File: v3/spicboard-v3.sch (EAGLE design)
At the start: 37 parts, among them IC1 74HC595N, Q1 BC557, Q2 BC557

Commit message: Zwischenstand LEDs
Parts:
- removed BUTTON0, BUTTON1: MOMENTARY-SWITCH-SPST-PTH-6.0MM, spicboard-v3:MOMENTARY-SWITCH-SPST-PTH-6.0MM
- added BTN0, BTN1: (no value), switch-omron:10-XX
- added R13, R14: 330, resistor:R-EU_0207/10
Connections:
- new net N$15: COM.1, R14.2
- new net N$21: COM.3, R13.2
- net BTN1: now also BTN1.S, BTN1.S1; no longer BUTTON1.2
- net GND: now also BTN0.P, BTN0.P1, BTN1.P, BTN1.P1; no longer BUTTON0.1, BUTTON1.1
- net N$19: now also BTN0.S, BTN0.S1; no longer BUTTON0.2
- net RX: now also R13.1; no longer COM.3
- net TX: now also R14.1; no longer COM.1
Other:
- moved on the sheet: COM, OLED2
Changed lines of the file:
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@@
 <part name="IC1" library="74xx-eu" deviceset="74*595" device="N" technology="HC"/>
 <part name="LDR" library="spicboard-v3" deviceset="LDR" device="LDR" value=""/>
-<part name="BUTTON0" library="spicboard-v3" deviceset="MOMENTARY-SWITCH-SPST" device="-PTH-6.0MM" value=""/>
-<part name="BUTTON1" library="spicboard-v3" deviceset="MOMENTARY-SWITCH-SPST" device="-PTH-6.0MM" value=""/>
 <part name="VR1" library="spicboard-v3" deviceset="POTENTIOMETER" device="-PTH-9MM-1/20W-20%" value="10k"/>
 <part name="RN1" library="resistor-sil" deviceset="E4R" device=""/>
@@
 <part name="OLED2" library="pinhead" deviceset="PINHD-1X4" device=""/>
 <part name="COM" library="pinhead" deviceset="PINHD-1X3" device=""/>
+<part name="R13" library="resistor" deviceset="R-EU_" device="0207/10" value="330"/>
+<part name="R14" library="resistor" deviceset="R-EU_" device="0207/10" value="330"/>
+<part name="BTN0" library="switch-omron" deviceset="10-XX" device=""/>
+<part name="BTN1" library="switch-omron" deviceset="10-XX" device=""/>
 </parts>
 <sheets>
@@
 <instance part="IC1" gate="A" x="109.22" y="40.64"/>
 <instance part="LDR" gate="G$1" x="83.82" y="101.6" rot="R90"/>
-<instance part="BUTTON0" gate="G$1" x="129.54" y="0" rot="R90"/>
-<instance part="BUTTON1" gate="G$1" x="172.72" y="0" rot="R90"/>
 <instance part="VR1" gate="G$1" x="63.5" y="96.52" rot="MR0"/>
 <instance part="RN1" gate="A" x="139.7" y="48.26"/>
@@
 <instance part="EXT" gate="A" x="48.26" y="-20.32"/>
 <instance part="OLED1" gate="A" x="48.26" y="-2.54"/>
-<instance part="OLED2" gate="A" x="68.58" y="-2.54"/>
-<instance part="COM" gate="A" x="68.58" y="-17.78"/>
+<instance part="OLED2" gate="A" x="81.28" y="-2.54"/>
+<instance part="COM" gate="A" x="81.28" y="-17.78"/>
+<instance part="R13" gate="G$1" x="68.58" y="-20.32"/>
+<instance part="R14" gate="G$1" x="68.58" y="-15.24"/>
+<instance part="BTN0" gate="1" x="129.54" y="0"/>
+<instance part="BTN1" gate="1" x="172.72" y="0"/>
 </instances>
 <busses>
@@
 <segment>
 <pinref part="OLED2" gate="A" pin="1"/>
-<wire x1="66.04" y1="2.54" x2="50.8" y2="2.54" width="0.1524" layer="91"/>
-<label x="50.8" y="2.54" size="1.778" layer="95"/>
+<wire x1="78.74" y1="2.54" x2="63.5" y2="2.54" width="0.1524" layer="91"/>
+<label x="63.5" y="2.54" size="1.778" layer="95"/>
 </segment>
 <segment>
@@
 </segment>
 <segment>
-<pinref part="BUTTON0" gate="G$1" pin="1"/>
 <wire x1="129.54" y1="-5.08" x2="129.54" y2="-7.62" width="0.1524" layer="91"/>
 <pinref part="GND7" gate="1" pin="GND"/>
-<wire x1="129.54" y1="-7.62" x2="137.16" y2="-7.62" width="0.1524" layer="91"/>
+<wire x1="129.54" y1="-7.62" x2="132.08" y2="-7.62" width="0.1524" layer="91"/>
+<wire x1="132.08" y1="-7.62" x2="137.16" y2="-7.62" width="0.1524" layer="91"/>
 <wire x1="137.16" y1="-7.62" x2="144.78" y2="-7.62" width="0.1524" layer="91"/>
 <junction x="137.16" y="-7.62"/>
@@
 <wire x1="144.78" y1="-7.62" x2="144.78" y2="-2.54" width="0.1524" layer="91"/>
 <wire x1="144.78" y1="-7.62" x2="172.72" y2="-7.62" width="0.1524" layer="91"/>
-<pinref part="BUTTON1" gate="G$1" pin="1"/>
 <wire x1="172.72" y1="-7.62" x2="172.72" y2="-5.08" width="0.1524" layer="91"/>
+<pinref part="BTN0" gate="1" pin="P"/>
+<pinref part="BTN1" gate="1" pin="P"/>
+<pinref part="BTN0" gate="1" pin="P1"/>
+<wire x1="132.08" y1="-5.08" x2="132.08" y2="-7.62" width="0.1524" layer="91"/>
+<junction x="132.08" y="-7.62"/>
+<pinref part="BTN1" gate="1" pin="P1"/>
+<wire x1="175.26" y1="-5.08" x2="175.26" y2="-7.62" width="0.1524" layer="91"/>
+<wire x1="175.26" y1="-7.62" x2="172.72" y2="-7.62" width="0.1524" layer="91"/>
+<junction x="172.72" y="-7.62"/>
 </segment>
 <segment>
@@
 <segment>
 <pinref part="OLED2" gate="A" pin="2"/>
-<wire x1="66.04" y1="0" x2="50.8" y2="0" width="0.1524" layer="91"/>
-<label x="50.8" y="0" size="1.778" layer="95"/>
+<wire x1="78.74" y1="0" x2="63.5" y2="0" width="0.1524" layer="91"/>
+<label x="63.5" y="0" size="1.778" layer="95"/>
 </segment>
 <segment>
 <pinref part="COM" gate="A" pin="2"/>
-<wire x1="66.04" y1="-17.78" x2="50.8" y2="-17.78" width="0.1524" layer="91"/>
-<label x="50.8" y="-17.78" size="1.778" layer="95"/>
+<wire x1="78.74" y1="-17.78" x2="55.88" y2="-17.78" width="0.1524" layer="91"/>
+<label x="55.88" y="-17.78" size="1.778" layer="95"/>
 </segment>
 <segment>
@@
 <net name="N$19" class="0">
 <segment>
-<pinref part="BUTTON0" gate="G$1" pin="2"/>
 <wire x1="129.54" y1="5.08" x2="129.54" y2="7.62" width="0.1524" layer="91"/>
 <pinref part="R12" gate="G$1" pin="1"/>
 <wire x1="129.54" y1="7.62" x2="132.08" y2="7.62" width="0.1524" layer="91"/>
+<pinref part="BTN0" gate="1" pin="S"/>
+<pinref part="BTN0" gate="1" pin="S1"/>
+<wire x1="132.08" y1="5.08" x2="132.08" y2="7.62" width="0.1524" layer="91"/>
+<junction x="132.08" y="7.62"/>
 </segment>
 </net>
@@
 <net name="BTN1" class="0">
 <segment>
-<pinref part="BUTTON1" gate="G$1" pin="2"/>
 <wire x1="172.72" y1="5.08" x2="172.72" y2="7.62" width="0.1524" layer="91"/>
-<wire x1="172.72" y1="7.62" x2="182.88" y2="7.62" width="0.1524" layer="91"/>
+<wire x1="172.72" y1="7.62" x2="175.26" y2="7.62" width="0.1524" layer="91"/>
 <label x="175.26" y="7.62" size="1.778" layer="95"/>
+<pinref part="BTN1" gate="1" pin="S"/>
+<pinref part="BTN1" gate="1" pin="S1"/>
+<wire x1="175.26" y1="7.62" x2="182.88" y2="7.62" width="0.1524" layer="91"/>
+<wire x1="175.26" y1="5.08" x2="175.26" y2="7.62" width="0.1524" layer="91"/>
+<junction x="175.26" y="7.62"/>
 </segment>
 <segment>
@@
 <net name="TX" class="0">
 <segment>
-<pinref part="COM" gate="A" pin="1"/>
-<wire x1="66.04" y1="-15.24" x2="50.8" y2="-15.24" width="0.1524" layer="91"/>
-<label x="50.8" y="-15.24" size="1.778" layer="95"/>
+<label x="55.88" y="-15.24" size="1.778" layer="95"/>
+<pinref part="R14" gate="G$1" pin="1"/>
+<wire x1="63.5" y1="-15.24" x2="55.88" y2="-15.24" width="0.1524" layer="91"/>
 </segment>
 <segment>
@@
 <net name="RX" class="0">
 <segment>
-<pinref part="COM" gate="A" pin="3"/>
-<wire x1="66.04" y1="-20.32" x2="50.8" y2="-20.32" width="0.1524" layer="91"/>
-<label x="50.8" y="-20.32" size="1.778" layer="95"/>
+<label x="55.88" y="-20.32" size="1.778" layer="95"/>
+<pinref part="R13" gate="G$1" pin="1"/>
+<wire x1="63.5" y1="-20.32" x2="55.88" y2="-20.32" width="0.1524" layer="91"/>
 </segment>
 <segment>
@@
 <segment>
 <pinref part="OLED2" gate="A" pin="4"/>
-<wire x1="66.04" y1="-5.08" x2="50.8" y2="-5.08" width="0.1524" layer="91"/>
-<label x="50.8" y="-5.08" size="1.778" layer="95"/>
+<wire x1="78.74" y1="-5.08" x2="63.5" y2="-5.08" width="0.1524" layer="91"/>
+<label x="63.5" y="-5.08" size="1.778" layer="95"/>
 </segment>
 </net>
@@
 <segment>
 <pinref part="OLED2" gate="A" pin="3"/>
-<wire x1="66.04" y1="-2.54" x2="50.8" y2="-2.54" width="0.1524" layer="91"/>
-<label x="50.8" y="-2.54" size="1.778" layer="95"/>
+<wire x1="78.74" y1="-2.54" x2="63.5" y2="-2.54" width="0.1524" layer="91"/>
+<label x="63.5" y="-2.54" size="1.778" layer="95"/>
 </segment>
 </net>
@@
 </segment>
 </net>
+<net name="N$15" class="0">
+<segment>
+<pinref part="COM" gate="A" pin="1"/>
+<wire x1="78.74" y1="-15.24" x2="73.66" y2="-15.24" width="0.1524" layer="91"/>
+<pinref part="R14" gate="G$1" pin="2"/>
+</segment>
+</net>
+<net name="N$21" class="0">
+<segment>
+<pinref part="COM" gate="A" pin="3"/>
+<wire x1="78.74" y1="-20.32" x2="73.66" y2="-20.32" width="0.1524" layer="91"/>
+<pinref part="R13" gate="G$1" pin="2"/>
+</segment>
+</net>

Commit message: Routing Zwischenstand
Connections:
- net IRQ renamed EXTIRQ
- removed net ADC: EXT.4
- new net EXTADC: B1.A3, EXT.4
- net L0: now also B1.*D6
- net L1: now also B1.*D5
- net L2: now also B1.D4
- net L3: now also B1.D7
- net L4: now also B1.D8
- net L5: now also B1.*D9
- net L6: now also B1.D12
- net L7: now also B1.A2
- net SS: now also IC1A.RCK
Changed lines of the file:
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@@
 <label x="22.86" y="78.74" size="1.778" layer="95"/>
+</segment>
+<segment>
+<pinref part="B1" gate="G$1" pin="*D6"/>
+<wire x1="76.2" y1="48.26" x2="83.82" y2="48.26" width="0.1524" layer="91"/>
+<label x="78.74" y="48.26" size="1.778" layer="95"/>
 </segment>
 </net>
@@
 <label x="22.86" y="71.12" size="1.778" layer="95"/>
 </segment>
+<segment>
+<pinref part="B1" gate="G$1" pin="*D5"/>
+<wire x1="76.2" y1="50.8" x2="83.82" y2="50.8" width="0.1524" layer="91"/>
+<label x="78.74" y="50.8" size="1.778" layer="95"/>
+</segment>
 </net>
 <net name="L2" class="0">
@@
 <label x="22.86" y="63.5" size="1.778" layer="95"/>
 </segment>
+<segment>
+<pinref part="B1" gate="G$1" pin="D4"/>
+<wire x1="76.2" y1="53.34" x2="83.82" y2="53.34" width="0.1524" layer="91"/>
+<label x="78.74" y="53.34" size="1.778" layer="95"/>
+</segment>
 </net>
 <net name="L3" class="0">
@@
 <label x="22.86" y="55.88" size="1.778" layer="95"/>
 </segment>
+<segment>
+<pinref part="B1" gate="G$1" pin="D7"/>
+<wire x1="76.2" y1="45.72" x2="83.82" y2="45.72" width="0.1524" layer="91"/>
+<label x="78.74" y="45.72" size="1.778" layer="95"/>
+</segment>
 </net>
 <net name="L4" class="0">
@@
 <label x="22.86" y="48.26" size="1.778" layer="95"/>
 </segment>
+<segment>
+<pinref part="B1" gate="G$1" pin="D8"/>
+<wire x1="76.2" y1="43.18" x2="83.82" y2="43.18" width="0.1524" layer="91"/>
+<label x="78.74" y="43.18" size="1.778" layer="95"/>
+</segment>
 </net>
 <net name="L5" class="0">
@@
 <label x="22.86" y="40.64" size="1.778" layer="95"/>
 </segment>
+<segment>
+<pinref part="B1" gate="G$1" pin="*D9"/>
+<wire x1="76.2" y1="40.64" x2="83.82" y2="40.64" width="0.1524" layer="91"/>
+<label x="78.74" y="40.64" size="1.778" layer="95"/>
+</segment>
 </net>
 <net name="L6" class="0">
@@
 <label x="22.86" y="33.02" size="1.778" layer="95"/>
 </segment>
+<segment>
+<pinref part="B1" gate="G$1" pin="D12"/>
+<wire x1="76.2" y1="33.02" x2="83.82" y2="33.02" width="0.1524" layer="91"/>
+<label x="78.74" y="33.02" size="1.778" layer="95"/>
+</segment>
 </net>
 <net name="L7" class="0">
@@
 <wire x1="20.32" y1="25.4" x2="25.4" y2="25.4" width="0.1524" layer="91"/>
 <label x="22.86" y="25.4" size="1.778" layer="95"/>
+</segment>
+<segment>
+<pinref part="B1" gate="G$1" pin="A2"/>
+<wire x1="50.8" y1="60.96" x2="35.56" y2="60.96" width="0.1524" layer="91"/>
+<label x="35.56" y="60.96" size="1.778" layer="95"/>
 </segment>
 </net>
@@
 </segment>
 </net>
-<net name="IRQ" class="0">
+<net name="EXTIRQ" class="0">
 <segment>
 <pinref part="EXT" gate="A" pin="3"/>
@@
 </segment>
 </net>
-<net name="ADC" class="0">
+<net name="EXTADC" class="0">
 <segment>
 <pinref part="EXT" gate="A" pin="4"/>
 <wire x1="45.72" y1="-22.86" x2="27.94" y2="-22.86" width="0.1524" layer="91"/>
 <label x="27.94" y="-22.86" size="1.778" layer="95"/>
+</segment>
+<segment>
+<pinref part="B1" gate="G$1" pin="A3"/>
+<wire x1="50.8" y1="58.42" x2="35.56" y2="58.42" width="0.1524" layer="91"/>
+<label x="35.56" y="58.42" size="1.778" layer="95"/>
 </segment>
 </net>
@@
 </segment>
 </net>
-<net name="SS" class="0">
-<segment>
-<pinref part="B1" gate="G$1" pin="*D10"/>
-<wire x1="76.2" y1="38.1" x2="86.36" y2="38.1" width="0.1524" layer="91"/>
-<label x="78.74" y="38.1" size="1.778" layer="95"/>
-<wire x1="86.36" y1="38.1" x2="99.06" y2="38.1" width="0.1524" layer="91"/>
-</segment>
-</net>
 <net name="N$15" class="0">
 <segment>
@@
 </segment>
 </net>
+<net name="SS" class="0">
+<segment>
+<pinref part="B1" gate="G$1" pin="*D10"/>
+<pinref part="IC1" gate="A" pin="RCK"/>
+<wire x1="76.2" y1="38.1" x2="96.52" y2="38.1" width="0.1524" layer="91"/>
+<label x="78.74" y="38.1" size="1.778" layer="95"/>
+</segment>
+</net>

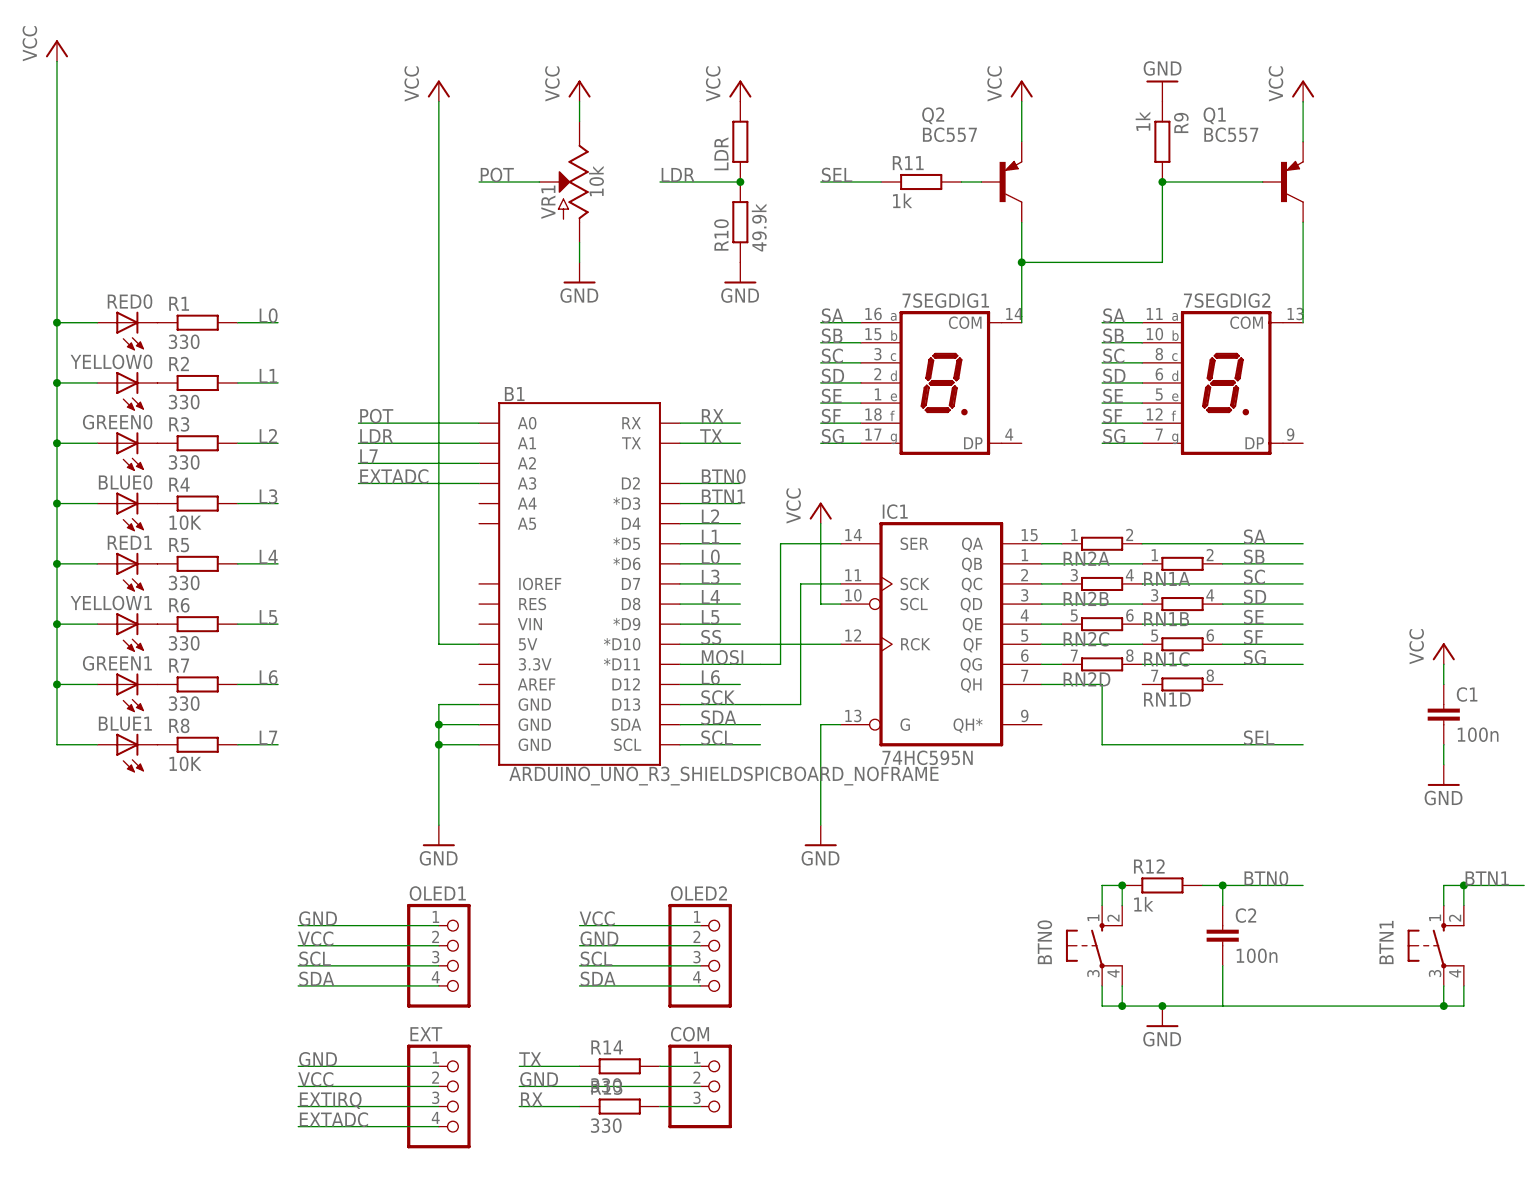
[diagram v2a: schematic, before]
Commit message: EXTIRQ auf BTN1, Werte für Widerstandsnetzwerke
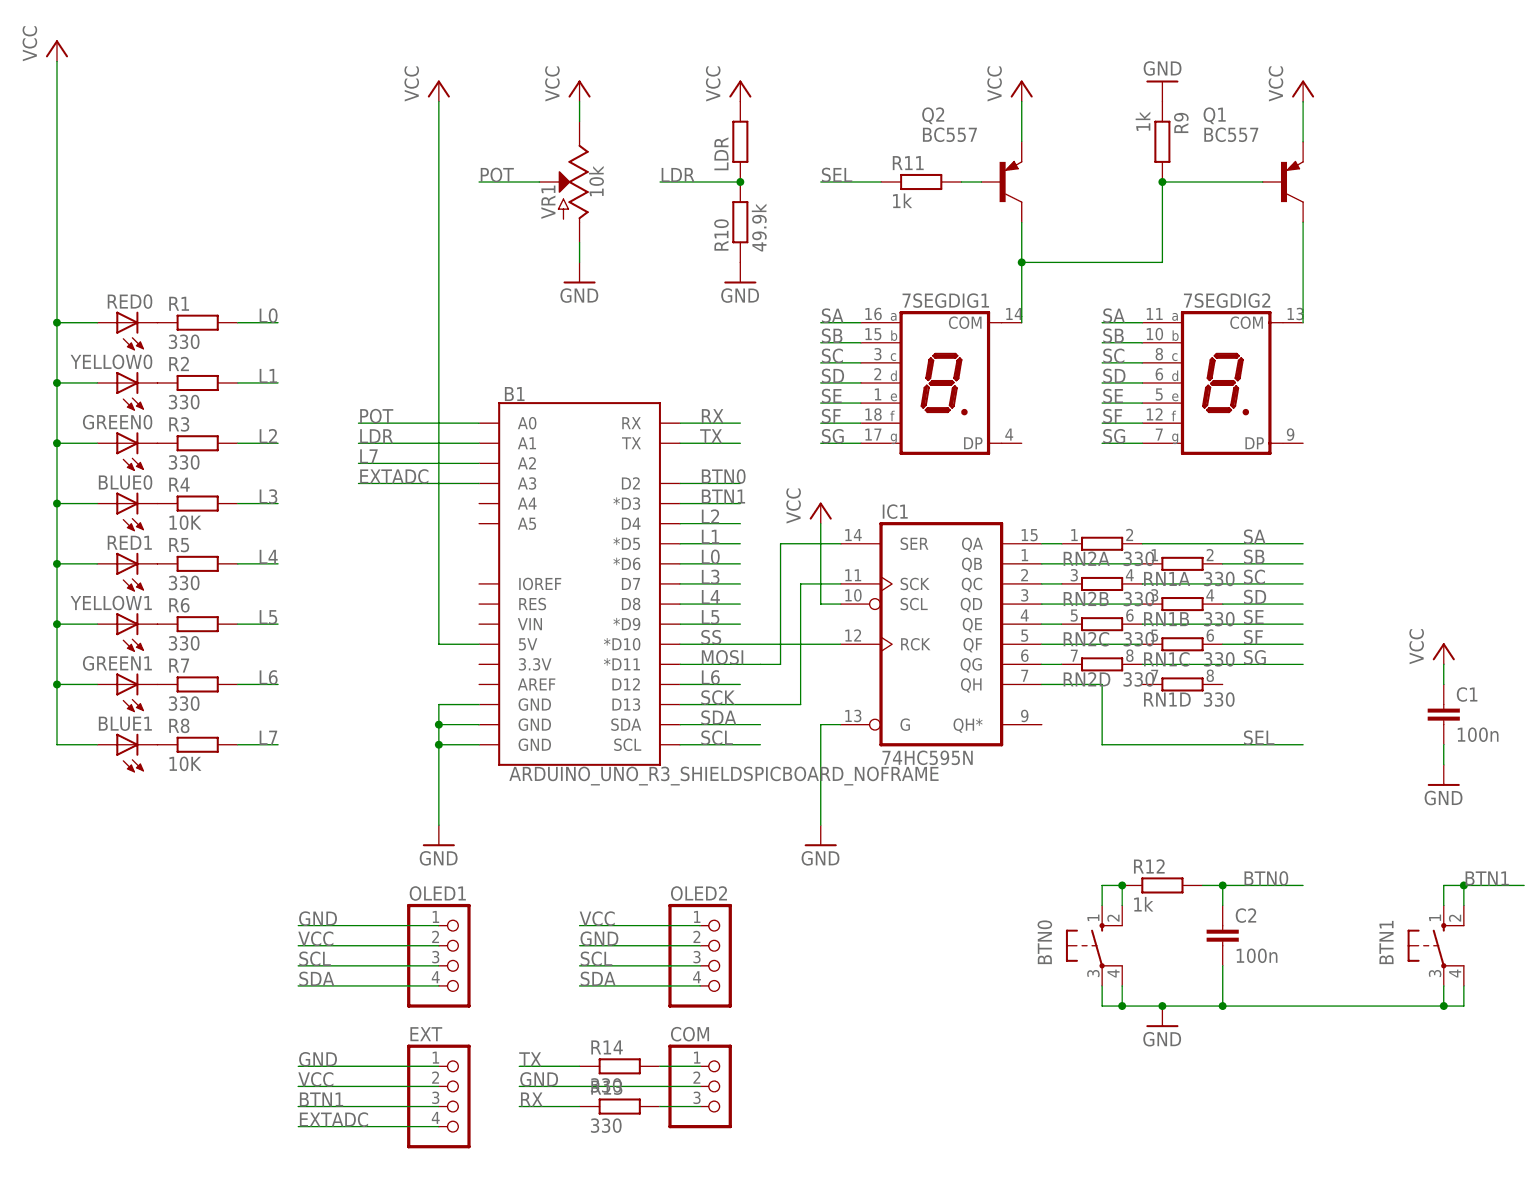
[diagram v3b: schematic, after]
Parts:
- RN1, RN2: value (none) -> 330
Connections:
- removed net EXTIRQ: EXT.3
- net BTN1: now also EXT.3
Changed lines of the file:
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@@
 <part name="LDR" library="spicboard-v3" deviceset="LDR" device="LDR" value=""/>
 <part name="VR1" library="spicboard-v3" deviceset="POTENTIOMETER" device="-PTH-9MM-1/20W-20%" value="10k"/>
-<part name="RN1" library="resistor-sil" deviceset="E4R" device=""/>
-<part name="RN2" library="resistor-sil" deviceset="E4R" device=""/>
+<part name="RN1" library="resistor-sil" deviceset="E4R" device="" value="330"/>
+<part name="RN2" library="resistor-sil" deviceset="E4R" device="" value="330"/>
 <part name="Q1" library="transistor-pnp" deviceset="BC557*" device=""/>
 <part name="Q2" library="transistor-pnp" deviceset="BC557*" device=""/>
@@
 <wire x1="175.26" y1="-7.62" x2="172.72" y2="-7.62" width="0.1524" layer="91"/>
 <junction x="172.72" y="-7.62"/>
+<junction x="144.78" y="-7.62"/>
 </segment>
 <segment>
@@
 <label x="78.74" y="55.88" size="1.778" layer="95"/>
 </segment>
-</net>
-<net name="EXTIRQ" class="0">
 <segment>
 <pinref part="EXT" gate="A" pin="3"/>
